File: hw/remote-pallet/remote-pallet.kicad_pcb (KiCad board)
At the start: 2 copper layers, 90 x 90 mm, 87 parts, among them J1 Power, M0 E-MATCH, M1 E-MATCH, M2 E-MATCH, M3 E-MATCH, M4 E-MATCH, M5 E-MATCH, M6 E-MATCH, M7 E-MATCH, Q1 EMatch Test, Q10 Q_PMOS_DGS, Q11 Q_NMOS_GDS, Q12 Q_PMOS_DGS, Q13 Q_NMOS_GDS, Q14 Q_PMOS_DGS, Q15 Q_NMOS_GDS, Q16 Q_PMOS_DGS, Q17 Q_NMOS_GDS, Q2 Q_PMOS_DGS, Q3 Q_NMOS_GDS, Q4 Q_PMOS_DGS, Q5 Q_NMOS_GDS, Q6 Q_PMOS_DGS, Q7 Q_NMOS_GDS, Q8 Q_PMOS_DGS, Q9 Q_NMOS_GDS, SW1 Power, SW2 Arm Hardware, U1 Photon Power, U2 PHOTON, U3 Armed Sense

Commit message: updating sch
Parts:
- moved G*** 127.0 mm to (167.6, 61.0)
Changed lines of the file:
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@@
     (links 163)
     (no_connects 0)
-    (area 91.949999 49.949999 182.050001 140.050001)
+    (area 42.270863 49.675 191.5 142.950001)
     (thickness 1.6)
     (drawings 10)
@@
   )
   (setup
-    (last_trace_width 0.3)
+    (last_trace_width 0.25)
     (user_trace_width 0.3)
     (user_trace_width 0.8)
@@
   (module M2011LL1W01-switch:M2011LL1W01 (layer F.Cu)
     (at 126.2 131.8 180)
-    (fp_text reference SW1 (at 5 -5.1 450) (layer F.SilkS)
-      (effects (font (size 1 1) (thickness 0.15)))
-    )
-    (fp_text value Power (at -5 -4.5 450) (layer F.Fab)
+    (fp_text reference SW1 (at 2.6 8.8 180) (layer F.SilkS)
+      (effects (font (size 1 1) (thickness 0.15)))
+    )
+    (fp_text value Power (at 2 7.4 360) (layer F.SilkS)
       (effects (font (size 1 1) (thickness 0.15)))
     )
@@
   (module M2011LL1W01-switch:M2011LL1W01 (layer F.Cu)
     (at 137.2 131.8 180)
-    (fp_text reference SW2 (at 5 -5.2 450) (layer F.SilkS)
-      (effects (font (size 1 1) (thickness 0.15)))
-    )
-    (fp_text value "Arm Hardware" (at -5 -1.4 450) (layer F.Fab)
+    (fp_text reference SW2 (at 2.6 8.8 180) (layer F.SilkS)
+      (effects (font (size 1 1) (thickness 0.15)))
+    )
+    (fp_text value "Arm Hardware" (at -1.2 7.4 360) (layer F.SilkS)
       (effects (font (size 1 1) (thickness 0.15)))
     )
@@
   )
   (module octopus:octopus (layer F.Cu)
-    (at 49 106.4)
+    (at 167.64 60.96)
     (fp_text reference G*** (at 0 0) (layer F.SilkS) hide
       (effects (font (thickness 0.3)))
@@
     )
   )
-  (gr_text OFF (at 58.9 131.8) (layer F.SilkS)
+  (gr_text OFF (at 142.6 127.4 90) (layer F.SilkS)
     (effects (font (size 1.5 1.5) (thickness 0.3)))
   )
-  (gr_text ARMED (at 50.7 131.8) (layer F.SilkS)
+  (gr_text ARMED (at 142.6 134.6 90) (layer F.SilkS)
     (effects (font (size 1.5 1.5) (thickness 0.3)))
   )
-  (gr_text OFF (at 58.5 127.2) (layer F.SilkS)
+  (gr_text OFF (at 121 127.4 90) (layer F.SilkS)
     (effects (font (size 1.5 1.5) (thickness 0.3)))
   )
-  (gr_text ON (at 48.3 127.2) (layer F.SilkS)
+  (gr_text ON (at 121 137 90) (layer F.SilkS)
     (effects (font (size 1.5 1.5) (thickness 0.3)))
   )

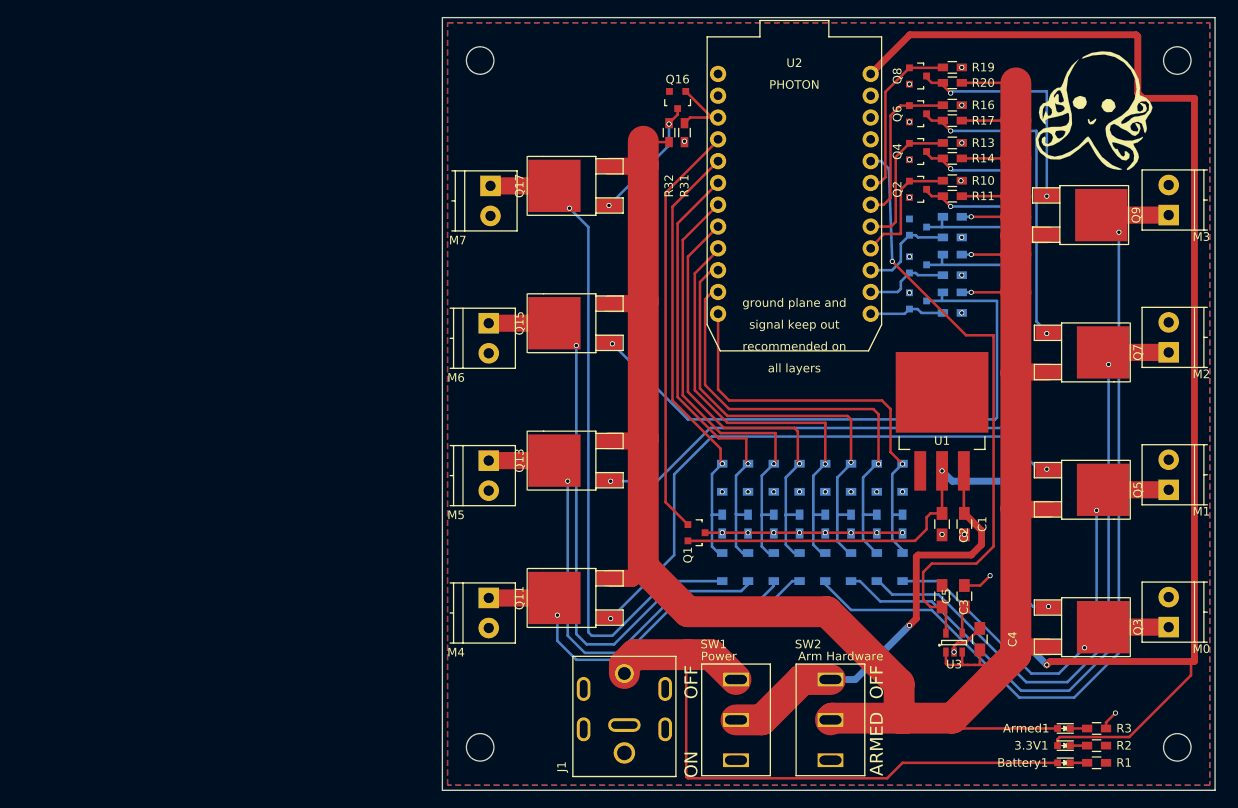
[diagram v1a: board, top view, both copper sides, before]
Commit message: updating pcb
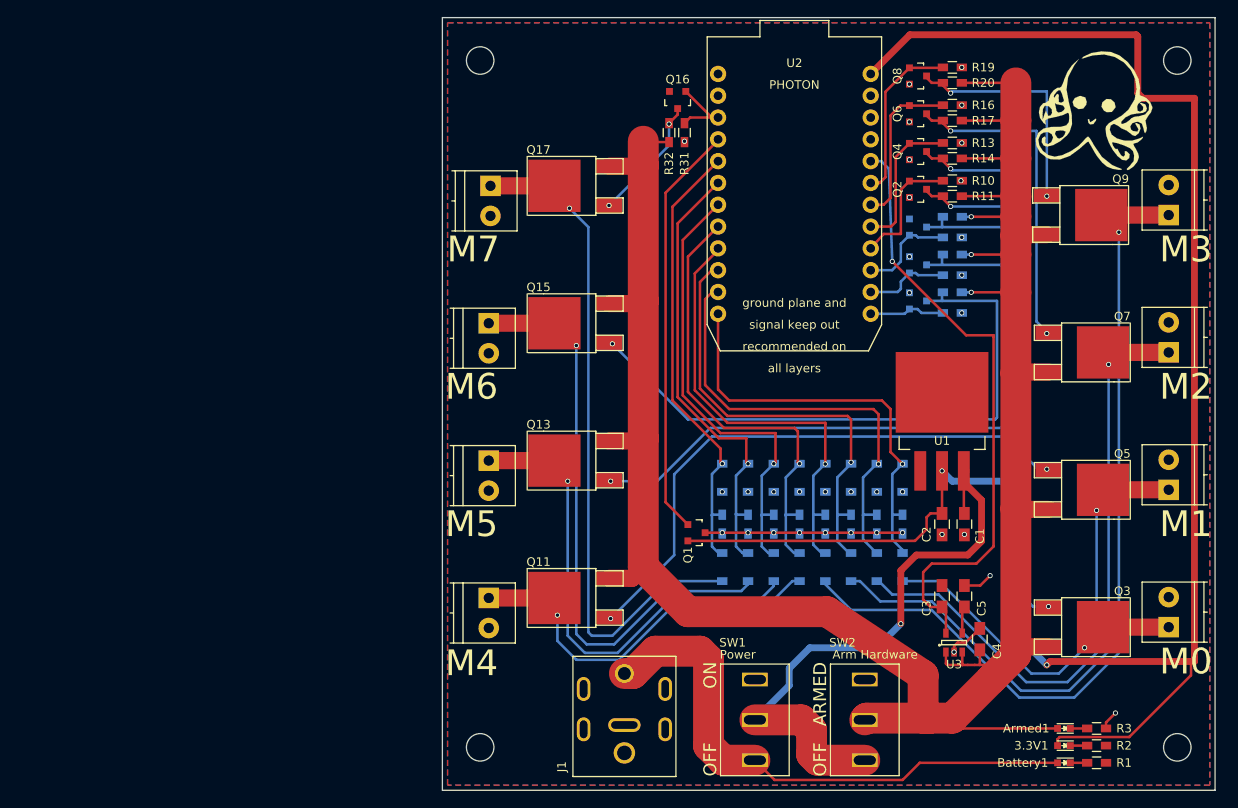
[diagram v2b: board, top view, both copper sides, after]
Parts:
- moved SW2 4.00 mm to (141.2, 131.8), turned to 0 degrees
- moved SW1 2.20 mm to (128.4, 131.8), turned to 0 degrees
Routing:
- net 12VSwitched: track 51.0 -> 70.5 mm
- net 12V: track 75.0 -> 65.2 mm
- net /ematch-0/VCC: track 305.5 -> 304.0 mm
